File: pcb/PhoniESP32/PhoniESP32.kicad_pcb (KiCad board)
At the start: 4 copper layers, 54 parts, among them J1 Connector, USB-TYPE-C-16P, J2 Conn_Battery, J3 Conn_Buttons, J4 Conn_01x08_Pin, J5 Screw_Terminal_01x02, SW1 SK12D07VG5, U1 TPS631000DRLR, U2 MAX98357AETE+T, U3 ESP32-C6-MINI-1-N4, U4 SPH0645LM4H-1-8_C19272537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

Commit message: feat(pcb): place test points and placeholders
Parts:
- added R19: 47kΩ, PCM_JLCPCB:R_0603, B.Cu at (135.6, 100.8)
- added R20: 0Ω, PCM_JLCPCB:R_0603, F.Cu at (135.6, 100.8)
- added R21: 0Ω, PCM_JLCPCB:R_0603, B.Cu at (159.9, 87.2)
- added R22: 0Ω, PCM_JLCPCB:R_0603, B.Cu at (162.6, 87.2)
- added TP1: TestPoint, TestPoint:TestPoint_Pad_D1.0mm, B.Cu at (144.2, 113.9)
- added TP10: TestPoint, TestPoint:TestPoint_Pad_D1.0mm, B.Cu at (159.8, 91.7)
- added TP11: TestPoint, TestPoint:TestPoint_Pad_D1.0mm, B.Cu at (154.8, 101.3)
- added TP2: TestPoint, TestPoint:TestPoint_Pad_D1.0mm, B.Cu at (154.8, 98.9)
- added TP3: TestPoint, TestPoint:TestPoint_Pad_D1.0mm, B.Cu at (141.3, 95.7)
- added TP4: TestPoint, TestPoint:TestPoint_Pad_D1.0mm, B.Cu at (138.7, 88.3)
- added TP5: TestPoint, TestPoint:TestPoint_Pad_D1.0mm, B.Cu at (137.8, 95.5)
- added TP6: TestPoint, TestPoint:TestPoint_Pad_D1.0mm, B.Cu at (157.2, 88.6)
- added TP7: TestPoint, TestPoint:TestPoint_Pad_D1.0mm, B.Cu at (163.0, 91.7)
- added TP8: TestPoint, TestPoint:TestPoint_Pad_D1.0mm, B.Cu at (165.1, 88.5)
- added TP9: TestPoint, TestPoint:TestPoint_Pad_D1.0mm, B.Cu at (162.6, 88.5)
- S1: value RESET -> Tactile Button, 160gf
- S2: value BOOT -> Tactile Button, 160gf
- moved J2 7.30 mm to (131.1, 109.4)
- moved SW1 1.63 mm to (134.3, 118.9)
- moved C1 1.10 mm to (134.3, 100.9)
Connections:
- U2 pad 2: unconnected-(U2-GAIN_SLOT-Pad2) -> Net-(U2-GAIN_SLOT)
- U5 pad 14: unconnected-(U5-TMR-Pad14) -> Net-(U5-TMR)
- U5 pad 15: GND -> Net-(U5-TD)

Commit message: feat(pcb): initial traces
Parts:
- added REF**: MountingHole_3.5mm, MountingHole:MountingHole_3.5mm, F.Cu at (125.0, 118.9)
- added REF**: MountingHole_3.5mm, MountingHole:MountingHole_3.5mm, F.Cu at (174.6, 90.3)
- added REF**: MountingHole_3.5mm, MountingHole:MountingHole_3.5mm, F.Cu at (124.9, 90.2)
- added REF**: MountingHole_3.5mm, MountingHole:MountingHole_3.5mm, F.Cu at (174.7, 118.9)
- R10, R11: footprint PCM_JLCPCB:R_0603 -> PCM_JLCPCB:R_0402
- moved TP4 44.5 mm to (175.8, 112.9)
- moved R13 25.8 mm to (126.9, 102.9)
- moved J2 12.2 mm to (123.8, 99.6), turned to 180 degrees
- moved U4 12.0 mm to (175.7, 96.3), turned to 0 degrees
- moved TP8 12.0 mm to (174.1, 96.4), turned to -90 degrees
- moved TP5 11.7 mm to (127.5, 101.0)
- moved C15 11.4 mm to (172.5, 96.2), turned to -90 degrees
- moved C14 10.9 mm to (173.5, 95.9), turned to -90 degrees
- moved C12 8.61 mm to (165.6, 88.5), turned to 90 degrees
- moved D2 7.38 mm to (123.7, 106.3)
- moved D3 7.38 mm to (123.7, 104.8)
- moved D4 7.38 mm to (123.8, 102.9)
- moved R6 7.38 mm to (126.5, 104.8)
- moved R7 7.38 mm to (126.5, 106.3)
- moved S1 7.06 mm to (133.0, 107.1)
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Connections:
- net Net-(D1-Pad1) renamed /Power/D-
- net Net-(D1-Pad3) renamed /Power/D+
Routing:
- net GND: track 0.00 -> 76.6 mm, vias 0 -> 88
- net +5V: track 0.00 -> 48.1 mm, vias 0 -> 2
- net /I2S_WS: track 0.00 -> 48.0 mm, vias 0 -> 4
- net VBUS: track 0.00 -> 43.9 mm, vias 0 -> 2
- net /SPI_MISO: track 0.00 -> 42.6 mm, vias 0 -> 2
- net Net-(U5-EN2): track 0.00 -> 39.4 mm, vias 0 -> 4
- net /AUDIO_EN: track 0.00 -> 37.2 mm, vias 0 -> 4
- net /BTN_VOL_UP: track 0.00 -> 36.7 mm, vias 0 -> 4
- net /RFID_EN: track 0.00 -> 35.8 mm
- net +3.3V: track 0.00 -> 35.0 mm, vias 0 -> 10
- net /SPI_MOSI: track 0.00 -> 34.6 mm, vias 0 -> 2
- net /SPI_SCK: track 0.00 -> 34.1 mm, vias 0 -> 2
- net /I2S_BCLK: track 0.00 -> 32.1 mm, vias 0 -> 4
- net Net-(U3-IO8): track 0.00 -> 31.4 mm, vias 0 -> 2
- net /CHARGER: track 0.00 -> 31.2 mm, vias 0 -> 3
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- added copper zone on In2.Cu, net +3.3V
- added copper zone on B.Cu, net GND
- added copper zone on F.Cu, net GND
- added copper zone on In1.Cu, net GND
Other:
- board outline added: 57.4 x 36.4 mm

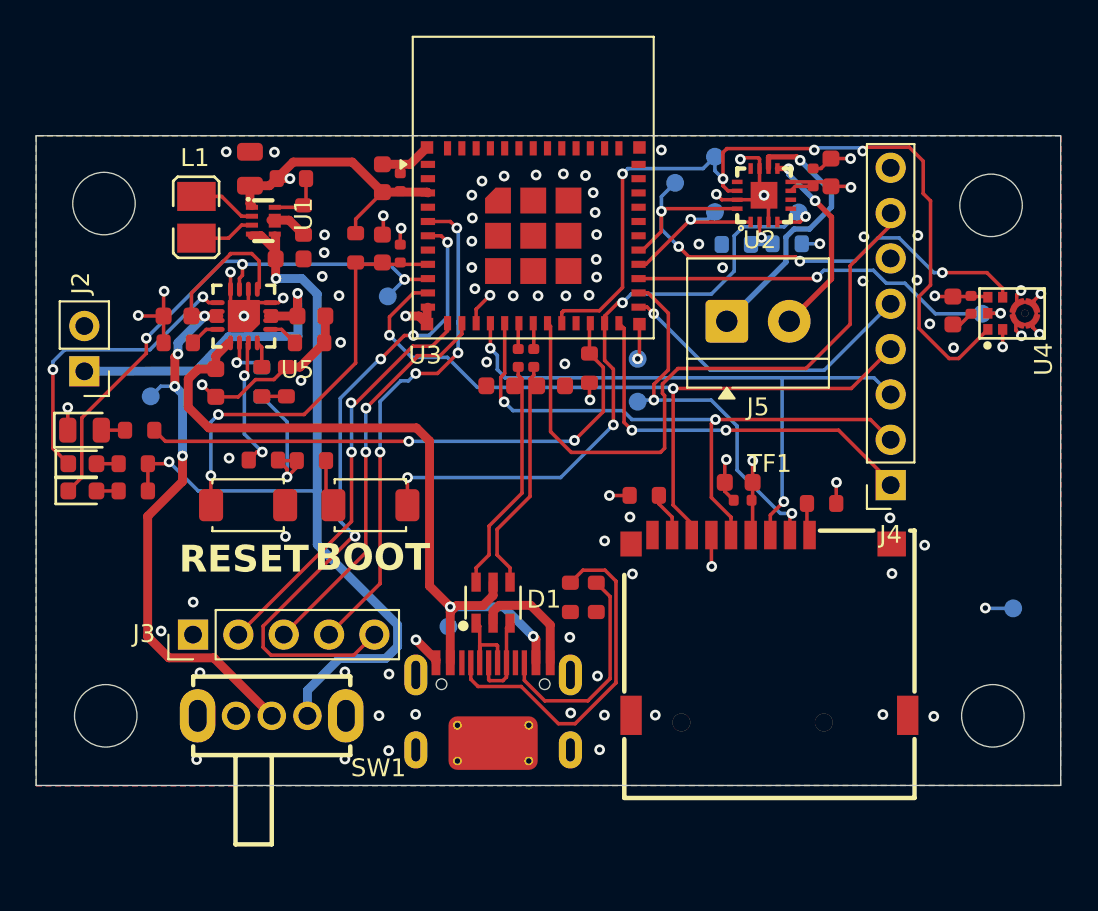
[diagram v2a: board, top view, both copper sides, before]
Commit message: chore(pcb): add bigger copper areas for power distribution
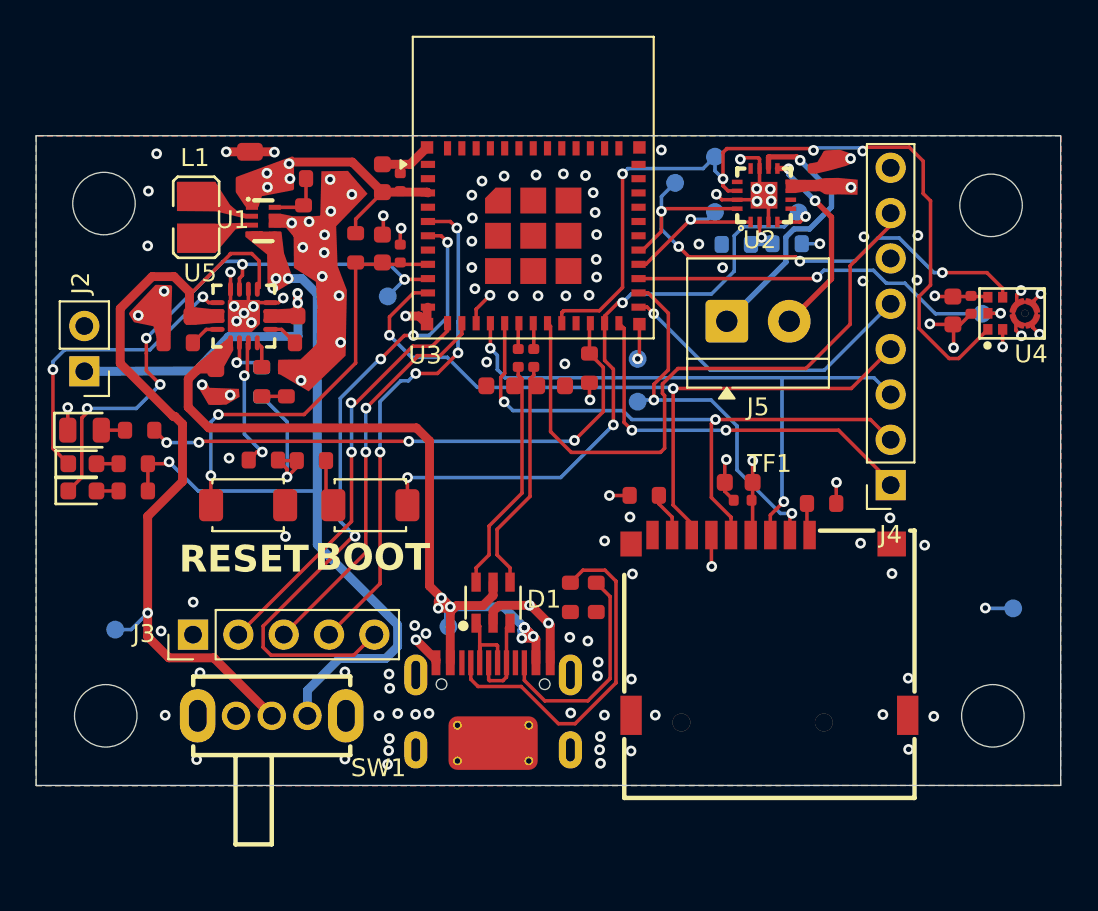
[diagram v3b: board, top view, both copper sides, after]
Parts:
- moved TP5 13.2 mm to (125.5, 114.1)
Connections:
- net Net-(U1-LX1) renamed /Power/LX1
- net Net-(U1-LX2) renamed /Power/LX2
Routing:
- net Net-(U5-EN2): track 39.4 -> 47.4 mm, vias 4 -> 1
- net /Power/LX2: track 3.57 -> 0.00 mm
- net /Power/LX1: track 3.41 -> 0.00 mm
- net GND: track 76.6 -> 74.1 mm, vias 88 -> 124
- net +3.3V: track 35.0 -> 32.5 mm, vias 10 -> 13
- net +5V: track 48.1 -> 50.5 mm, vias 2 -> 4
- net VBUS: track 43.9 -> 46.2 mm, vias 2 -> 7
- net /CHARGER: track 31.2 -> 33.4 mm, vias 3 -> 5
- net Net-(U3-IO8): track 31.4 -> 31.5 mm, vias 2 -> 4
- net Net-(J2-Pin_1): vias 1 -> 2

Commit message: chore(pcb): final cleanups
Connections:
- net Net-(J5-Pin_1) renamed /I2S/SPK-
- net Net-(J5-Pin_2) renamed /I2S/SPK+
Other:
- board text added: "+"
- board text added: "-"
- board text added: "Battery"
- board text added: "Buttons"
- board text added: "GND"
- board text added: "JLCJLCJLCJLC"
- board text added: "MFRC522"
- board text added: "PhoniESP32"
- board text added: "Speaker"
- board text added: "https://github.com/butzist/phoniesp32"

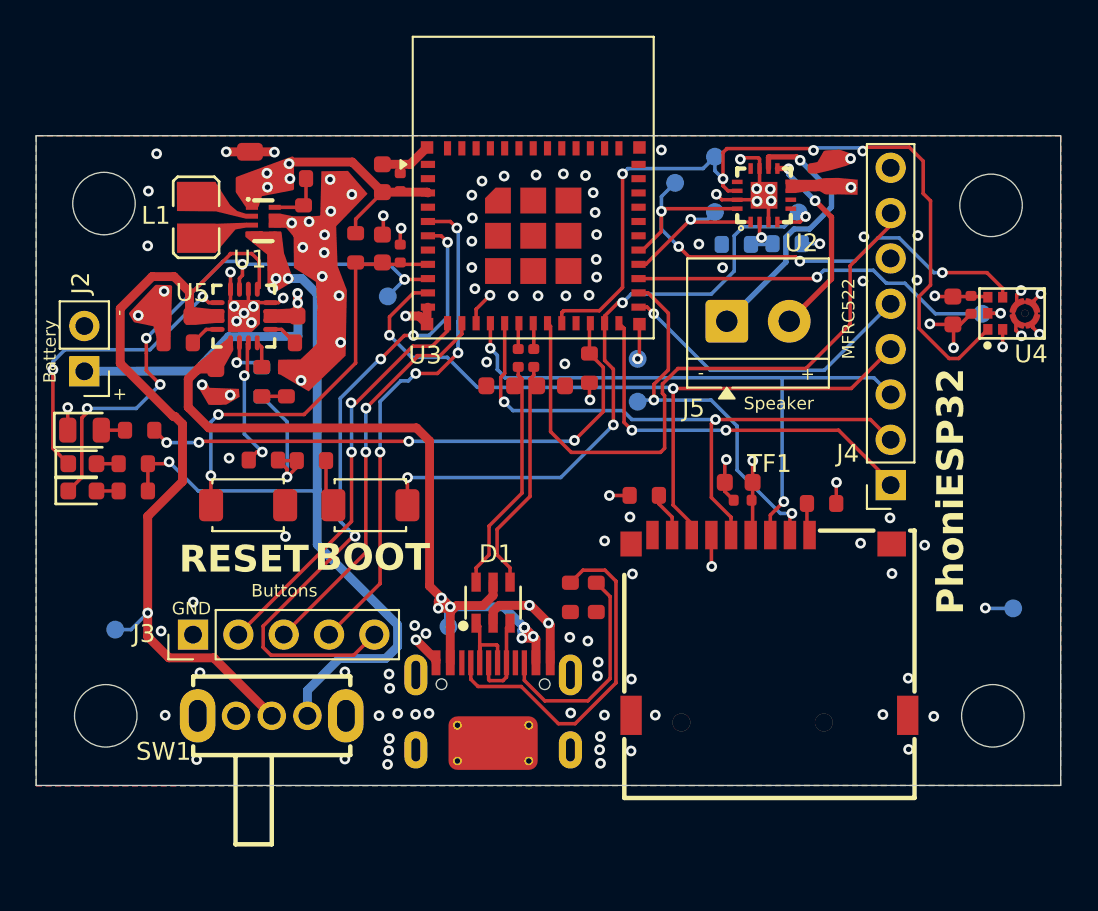
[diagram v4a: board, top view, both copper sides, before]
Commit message: fix(pcb): minor revisions by external reviewer
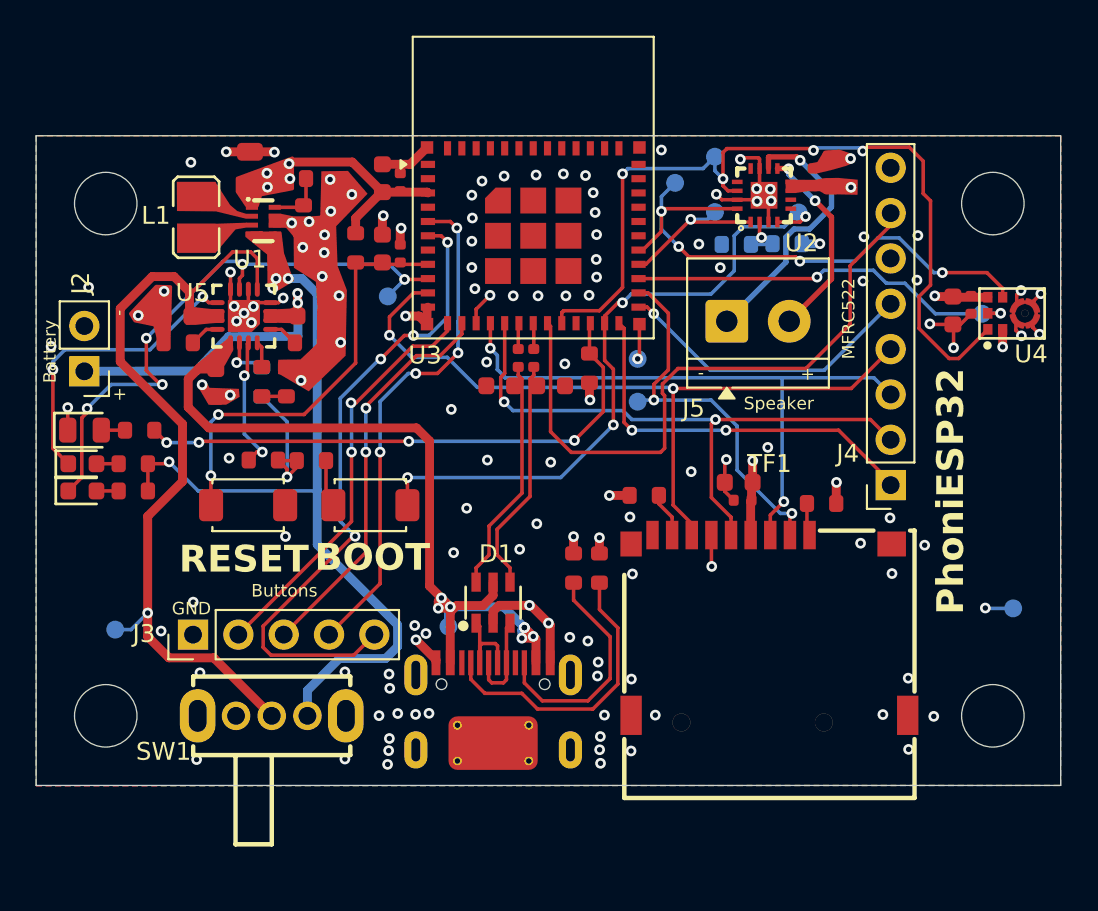
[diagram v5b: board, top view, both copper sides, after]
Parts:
- moved R1 2.31 mm to (152.7, 110.6), turned to 90 degrees
- moved R2 2.08 mm to (151.2, 110.6), turned to 90 degrees
- moved REF** 0.14 mm to (174.7, 90.2)
- moved REF** 0.10 mm to (125.0, 90.2)
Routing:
- net Net-(J1-CC1): track 19.8 -> 16.5 mm
- net GND: track 74.1 -> 76.0 mm, vias 124 -> 132
- net Net-(J1-CC2): track 12.5 -> 13.1 mm
